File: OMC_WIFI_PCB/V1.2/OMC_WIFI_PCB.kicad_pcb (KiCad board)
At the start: 2 copper layers, 148.6 x 75.9 mm, 20 parts, among them J1 Line Input, J10 Power, J11 Conn_01x06_Male, J12 Line Output, J13 Conn_01x06_Male, J2 Nuetral Input, J3 Neutral Output, J4 Switch, J5 Pins_FT232R, J8 Regulador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

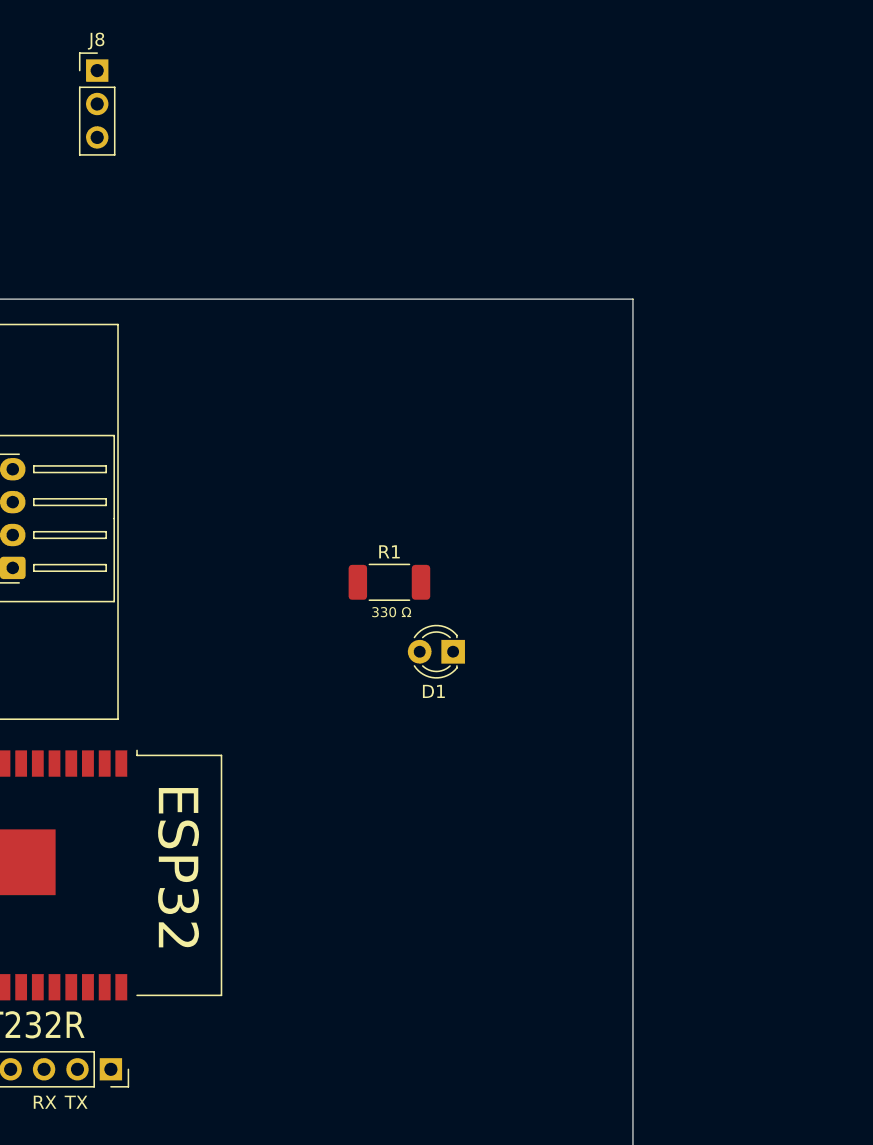
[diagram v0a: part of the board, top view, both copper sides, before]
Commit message: Actualización PCB y AutoConnect
> Cambios en código para compatibilidad entre clientes MQTT
> Agregados modelos 3D Fuente y Relay
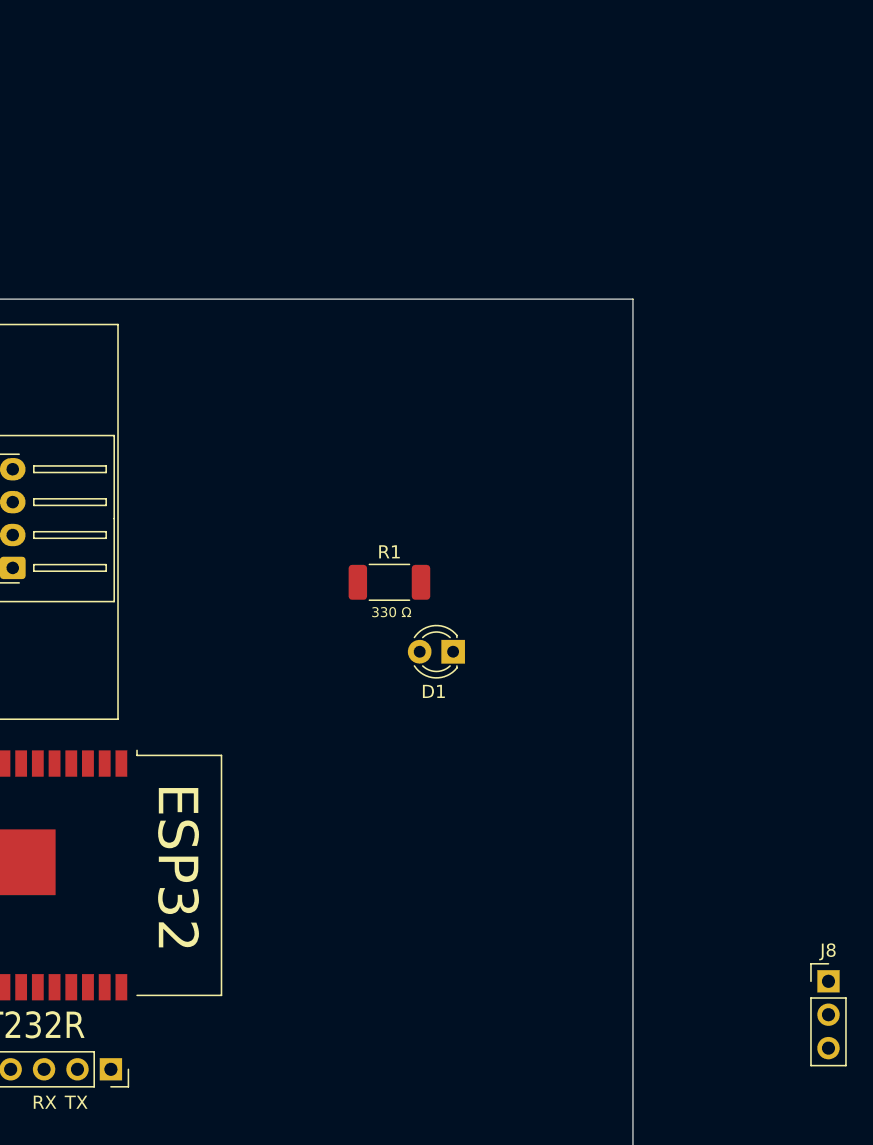
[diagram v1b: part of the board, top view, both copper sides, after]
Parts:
- moved J8 88.8 mm to (740.0, -930.1)

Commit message: Actualización PCB y nueva librería para plug macho
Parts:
- removed J2: Nuetral Input, omc-plugs:OMC-Male-Plug
- J1: value Line Input -> Conn_01x02_Male
- moved J1 14.0 mm to (583.0, -974.0)
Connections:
- J1 pad 2: (no net) -> NEUTRAL

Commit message: Actualización PCB y Librerías
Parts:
- removed J10: Power, TerminalBlock:TerminalBlock_bornier-4_P5.08mm
- removed J12: Line Output, omc-plugs:OMC-Female-Plug
- removed J3: Neutral Output, omc-plugs:OMC-Female-Plug
- removed J9: Datos, Connector_JST:JST_XH_S4B-XH-A-1_1x04_P2.50mm_Horizontal
- added D3: US1M, Diode_SMD:D_SMA, B.Cu at (598.8, -930.4)
- added J2: Conn_01x02_Female, omc-schematics LE:OMC-Female-Plug, F.Cu at (588.5, -962.1)
- added R3: 1k, Resistor_SMD:R_0603_1608Metric_Pad0.98x0.95mm_HandSolder, B.Cu at (593.2, -932.3)
- added U2: PZEM-004T-100A, omc-schematics LE:PZEM-OO4T-100A, F.Cu at (649.2, -965.9)
- D1: footprint LED_THT:LED_D3.0mm -> LED_SMD:LED_0603_1608Metric_Pad1.05x0.95mm_HandSolder
- D2: value US1M -> LED; footprint Diode_SMD:D_SMA -> LED_SMD:LED_0603_1608Metric_Pad1.05x0.95mm_HandSolder
- K1: footprint SLA-12VDC-SL-C:RELAY_SLA-12VDC-SL-C -> SLA-12VDC-SL-C LE:RELAY_SLA-12VDC-SL-C
- Q1: moved to B.Cu
- R1: footprint Resistor_SMD:R_2010_5025Metric_Pad1.40x2.65mm_HandSolder -> Resistor_SMD:R_0603_1608Metric_Pad0.98x0.95mm_HandSolder
- R2: value 1k -> 330; footprint Resistor_SMD:R_2010_5025Metric_Pad1.40x2.65mm_HandSolder -> Resistor_SMD:R_0603_1608Metric_Pad0.98x0.95mm_HandSolder
- moved D1 132.2 mm to (581.7, -930.1), turned to 0 degrees
- moved R1 124.6 mm to (585.8, -930.1)
- moved R2 63.3 mm to (585.6, -937.8)
- moved D2 63.1 mm to (581.7, -937.8)
- moved J8 57.9 mm to (689.4, -958.2)
- moved Q1 55.2 mm to (598.2, -934.3)
- moved J11 40.9 mm to (661.1, -918.8), turned to 270 degrees
- moved J13 40.4 mm to (661.1, -928.3), turned to 270 degrees
- moved J5 24.2 mm to (687.6, -947.5)
- moved J4 16.1 mm to (596.0, -924.0), turned to 180 degrees
- moved K1 8.25 mm to (613.0, -936.0)
- moved U1 5.86 mm to (681.0, -933.1), turned to 180 degrees
- moved PS1 3.61 mm to (638.0, -943.0)
- moved J1 1.40 mm to (581.6, -974.0)
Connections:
- net VN_ZMPT renamed Net-(U1-Pad5)
- net VP_ACS renamed Net-(U1-Pad4)
- D2 pad 1: +5V -> GND
- J1 pad 1: Net-(F1-Pad2) -> NEUTRAL
- J1 pad 2: NEUTRAL -> Net-(F1-Pad2)
- J11 pad 1: Net-(J11-Pad1) -> TX2_3V
- J11 pad 2: D32_RELAY_3V -> RX2_3V
- J11 pad 3: GND -> +3V
- J11 pad 4: +3V -> GND
- J11 pad 5: RX2_3V -> D32_RELAY_3V
- J11 pad 6: TX2_3V -> Net-(J11-Pad6)
- K1 pad C2: Net-(D2-Pad2) -> Net-(D3-Pad2)
- Q1 pad 3: Net-(D2-Pad2) -> Net-(D3-Pad2)
- R1 pad 1: D23_LED -> D22_LED_G
- R2 pad 1: D32_RELAY_5V -> D23_LED_R
- R2 pad 2: Net-(Q1-Pad2) -> Net-(D2-Pad2)
- U1 pad 33: Net-(U1-Pad33) -> D32_RELAY_3V
- U1 pad 36: Net-(U1-Pad36) -> D22_LED_G
- U1 pad 37: D23_LED -> D23_LED_R
- U1 pad 8: D32_RELAY_3V -> Net-(U1-Pad8)
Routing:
- net LINE_IN: track 74.1 -> 155.0 mm
- net Net-(J4-Pad1): track 0.00 -> 79.6 mm
- net D32_RELAY_5V: track 0.00 -> 76.9 mm
- net +5V: track 0.00 -> 53.2 mm
- net +3V: track 0.00 -> 36.6 mm, vias 0 -> 1
- net Net-(D3-Pad2): track 0.00 -> 31.1 mm
- net RX2_3V: track 0.00 -> 26.5 mm
- net TX2_3V: track 0.00 -> 24.2 mm
- net NEUTRAL: track 122.0 -> 109.4 mm
- net Net-(F1-Pad2): track 14.8 -> 26.3 mm
- net Net-(Q1-Pad2): track 0.00 -> 4.24 mm
- net LINE_OUT: track 11.6 -> 10.1 mm
- net RX0: track 0.62 -> 0.00 mm
- added copper zone on B.Cu, net GND
- added copper zone on F.Cu, net GND
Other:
- board size 148.6 x 75.9 mm -> 116 x 64.5 mm
- board text removed: "330 Ω"

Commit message: Actualización PCB
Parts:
- U1: moved to B.Cu
- moved J11 61.3 mm to (632.2, -972.9), turned to 90 degrees
- moved D1 57.3 mm to (530.0, -905.3)
- moved R1 57.3 mm to (534.1, -905.3)
- moved J4 57.3 mm to (544.3, -899.2)
- moved Q1 57.3 mm to (546.5, -909.5)
- moved R3 57.3 mm to (541.5, -907.5)
- moved D2 57.3 mm to (530.0, -913.0)
- moved D3 57.3 mm to (547.1, -905.6)
- moved R2 57.3 mm to (533.9, -913.0)
- moved J13 45.4 mm to (632.2, -963.4), turned to 90 degrees
- moved U1 44.5 mm to (659.0, -971.7)
- moved J5 19.5 mm to (672.6, -935.0), turned to 180 degrees
- moved J8 15.6 mm to (677.9, -947.7)
- moved U2 3.60 mm to (645.6, -965.8)
- moved F1 2.82 mm to (604.5, -958.3)
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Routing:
- net Net-(J4-Pad1): track 79.6 -> 0.00 mm
- net D32_RELAY_5V: track 76.9 -> 0.00 mm
- net +5V: track 53.2 -> 0.80 mm
- net LINE_IN: track 155.0 -> 107.7 mm
- net +3V: track 36.6 -> 0.00 mm, vias 1 -> 0
- net Net-(D3-Pad2): track 31.1 -> 0.00 mm
- net RX2_3V: track 26.5 -> 0.00 mm
- net Net-(F1-Pad2): track 26.3 -> 0.00 mm
- net TX2_3V: track 24.2 -> 0.00 mm
- net LINE_OUT: track 10.1 -> 23.6 mm
- net NEUTRAL: track 109.4 -> 101.3 mm
- net Net-(Q1-Pad2): track 4.24 -> 0.00 mm
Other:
- board size 116 x 64.5 mm -> 113 x 64.5 mm

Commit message: Actualización PCB
Diseño casi final
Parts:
- added C1: 1u, Capacitor_SMD:C_0603_1608Metric_Pad1.08x0.95mm_HandSolder, B.Cu at (671.8, -978.0)
- added J3: Conn_01x02_Male, Connector_PinHeader_2.54mm:PinHeader_1x02_P2.54mm_Vertical, F.Cu at (672.8, -937.0)
- added R4: 10k, Resistor_SMD:R_0603_1608Metric_Pad0.98x0.95mm_HandSolder, B.Cu at (674.9, -979.0)
- J11, J13: moved to B.Cu
- moved J4 125.1 mm to (666.5, -925.8), turned to 0 degrees
- moved R3 122.6 mm to (659.2, -941.8), turned to 270 degrees
- moved Q1 112.1 mm to (654.0, -941.5), turned to 180 degrees
- moved D3 111.1 mm to (654.2, -935.0), turned to 180 degrees
- moved D1 60.6 mm to (586.4, -927.4)
- moved D2 60.4 mm to (586.4, -934.8)
- moved R2 50.8 mm to (579.9, -934.8), turned to 180 degrees
- moved R1 50.8 mm to (579.9, -927.4), turned to 180 degrees
- moved J5 14.5 mm to (679.5, -947.8), turned to 0 degrees
- moved J8 5.15 mm to (672.8, -947.8)
- turned J11 to 270 degrees
- turned J13 to 270 degrees
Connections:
- D1 pad 1: GND -> Net-(D1-Pad1)
- D1 pad 2: Net-(D1-Pad2) -> D22_LED_G
- D2 pad 1: GND -> Net-(D2-Pad1)
- D2 pad 2: Net-(D2-Pad2) -> D23_LED_R
- J5 pad 1: DTR -> GND
- J5 pad 2: TX0 -> CTS
- J5 pad 3: RX0 -> VCC
- J5 pad 4: VCC -> RX0
- J5 pad 5: CTS -> TX0
- J5 pad 6: GND -> DTR
- R1 pad 1: D22_LED_G -> Net-(D1-Pad1)
- R1 pad 2: Net-(D1-Pad2) -> GND
- R2 pad 1: D23_LED_R -> Net-(D2-Pad1)
- R2 pad 2: Net-(D2-Pad2) -> GND
- U1 pad 2: +3V -> Net-(C1-Pad1)
- U1 pad 25: BOOT -> Net-(J3-Pad2)
- U1 pad 36: D22_LED_G -> D23_LED_R
- U1 pad 37: D23_LED_R -> D22_LED_G
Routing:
- net NEUTRAL: track 101.3 -> 257.9 mm
- net +5V: track 0.80 -> 150.9 mm
- net D23_LED_R: track 0.00 -> 148.6 mm, vias 0 -> 1
- net D22_LED_G: track 0.00 -> 148.1 mm, vias 0 -> 1
- net LINE_IN: track 107.7 -> 234.2 mm
- net Net-(D3-Pad2): track 0.00 -> 82.1 mm, vias 0 -> 2
- net +3V: track 0.00 -> 78.0 mm
- net TX0: track 0.00 -> 69.3 mm, vias 0 -> 1
- net RX0: track 0.00 -> 64.8 mm, vias 0 -> 1
- net Net-(F1-Pad2): track 0.00 -> 47.7 mm
- net RX2_5V: track 0.00 -> 44.2 mm
- net TX2_5V: track 0.00 -> 42.2 mm
- net Net-(J3-Pad2): track 0.00 -> 40.4 mm
- net D32_RELAY_5V: track 0.00 -> 27.7 mm
- net LINE_OUT: track 23.6 -> 47.2 mm
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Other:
- board size 113 x 64.5 mm -> 106.8 x 60 mm
- board text added: "3V"
- board text added: "5V"
- board text added: "GND"
- board text added: "PZEM-004T-100A"
- board text added: "SLA-05VDC"
- board text removed: "FT232R"

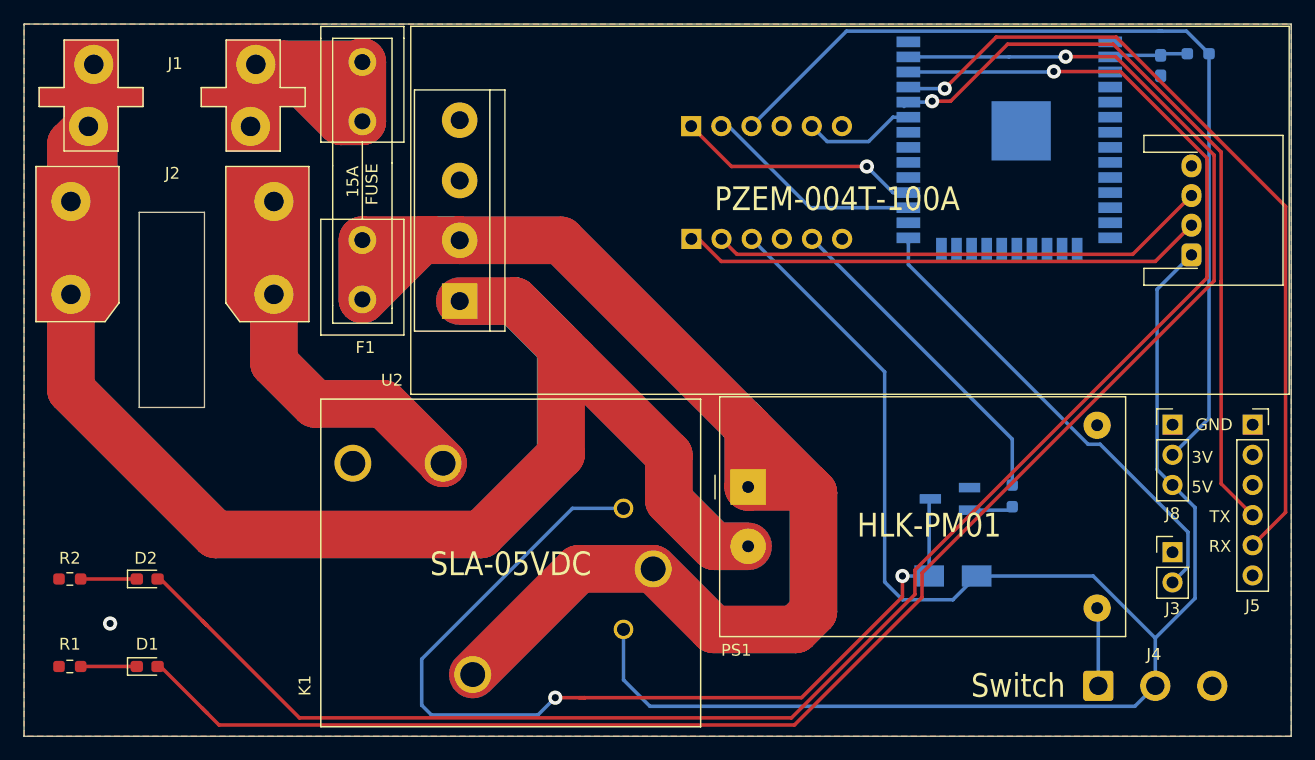
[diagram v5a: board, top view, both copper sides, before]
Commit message: Modelos 3D de clavijas
+Creación de modelos 3D para Clavijas
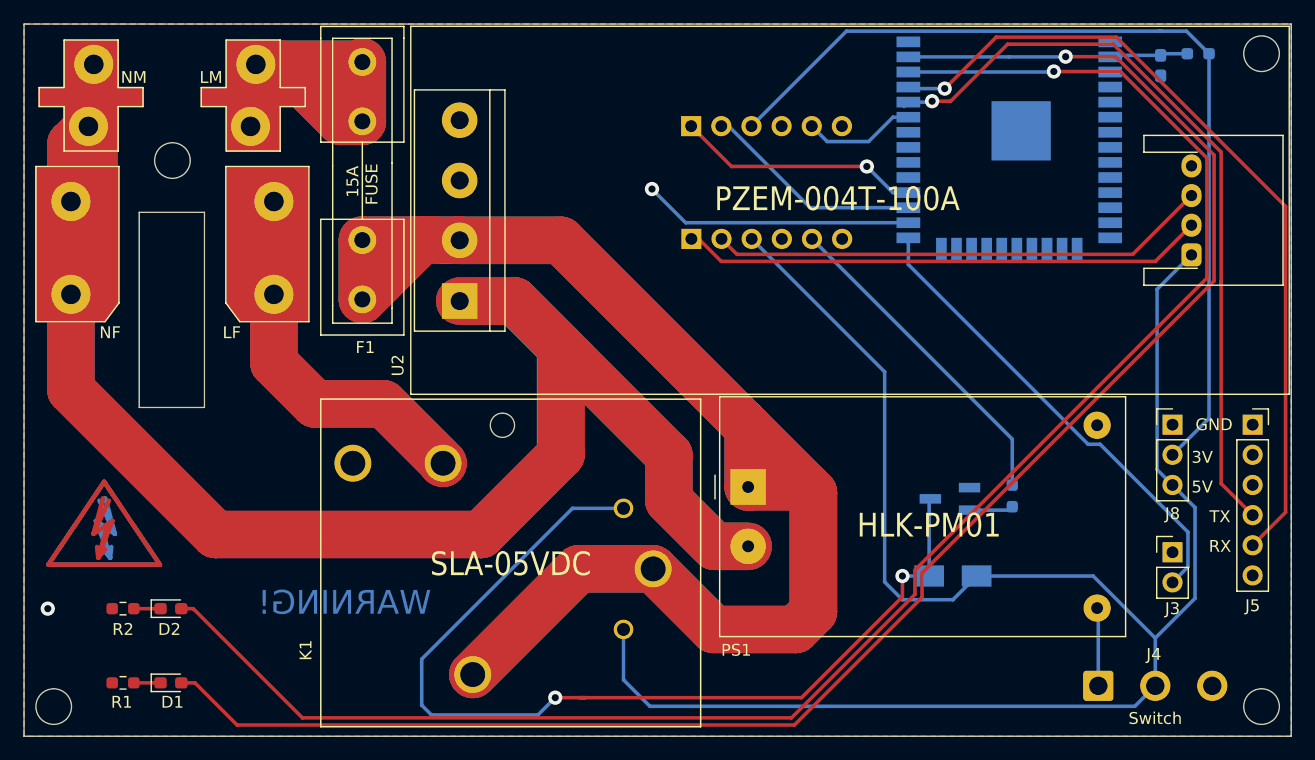
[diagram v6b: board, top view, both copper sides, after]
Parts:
- added SYM1: SYM_Flash_Small, Symbol:Symbol_HighVoltage_Type2_CopperTop_VerySmall, F.Cu at (582.8, -938.8)
- added SYM2: SYM_Flash_Small, Symbol:Symbol_HighVoltage_Type2_CopperTop_VerySmall, B.Cu at (582.8, -938.8)
- moved R2 5.13 mm to (584.3, -932.2)
- moved R1 4.69 mm to (584.3, -926.0)
- moved D2 3.20 mm to (588.4, -932.2)
- moved D1 2.43 mm to (588.4, -926.0)
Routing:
- net Net-(U1-Pad26): track 0.00 -> 22.8 mm, vias 0 -> 1
- net D23_LED_R: track 148.6 -> 145.1 mm
- net D22_LED_G: track 148.1 -> 145.0 mm
- net Net-(D2-Pad1): track 4.73 -> 2.50 mm
- net Net-(D1-Pad1): track 4.73 -> 2.50 mm
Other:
- outline, holes or cut-outs redrawn
- board text added: "LF"
- board text added: "LM"
- board text added: "NF"
- board text added: "NM"
- board text added: "WARNING!"

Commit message: Actualización PCB
> Creación de Versión 1.3 con espacio para toroide
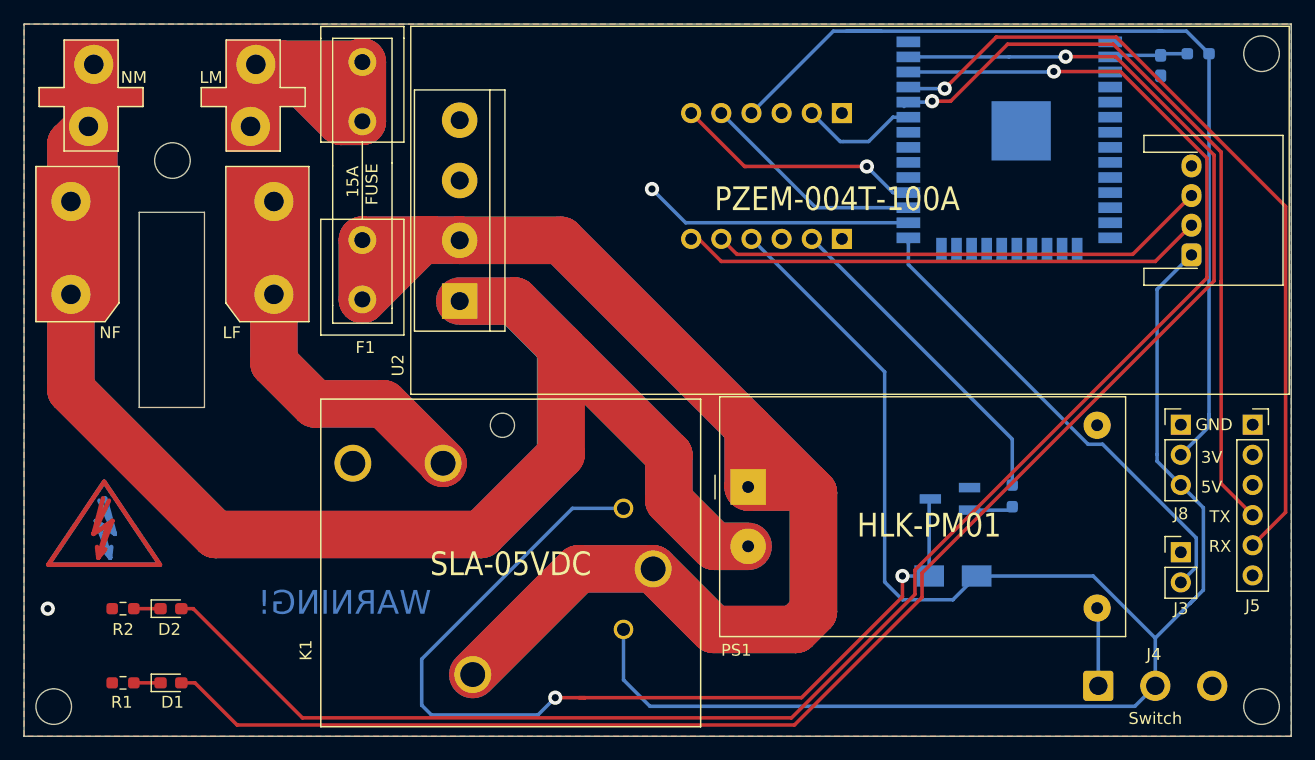
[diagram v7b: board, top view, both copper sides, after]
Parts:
- removed J11, J13: Conn_01x06_Male, Connector_PinHeader_2.54mm:PinHeader_1x06_P2.54mm_Vertical
- added J6: Level shifter, level_shifter:Level_Shifter_3V_5V, B.Cu at (638.7, -968.7)
- moved J3 0.70 mm to (673.5, -937.0)
- moved J8 0.70 mm to (673.5, -947.8)
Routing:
- net +3V: track 78.0 -> 80.4 mm
- net +5V: track 150.9 -> 152.2 mm
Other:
- board text added: "HV4"
- board text added: "LV1"
